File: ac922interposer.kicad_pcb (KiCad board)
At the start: 2 copper layers, 15 parts, among them J1 2336568-1, U1 molex_impact_85ohm_left_and_r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

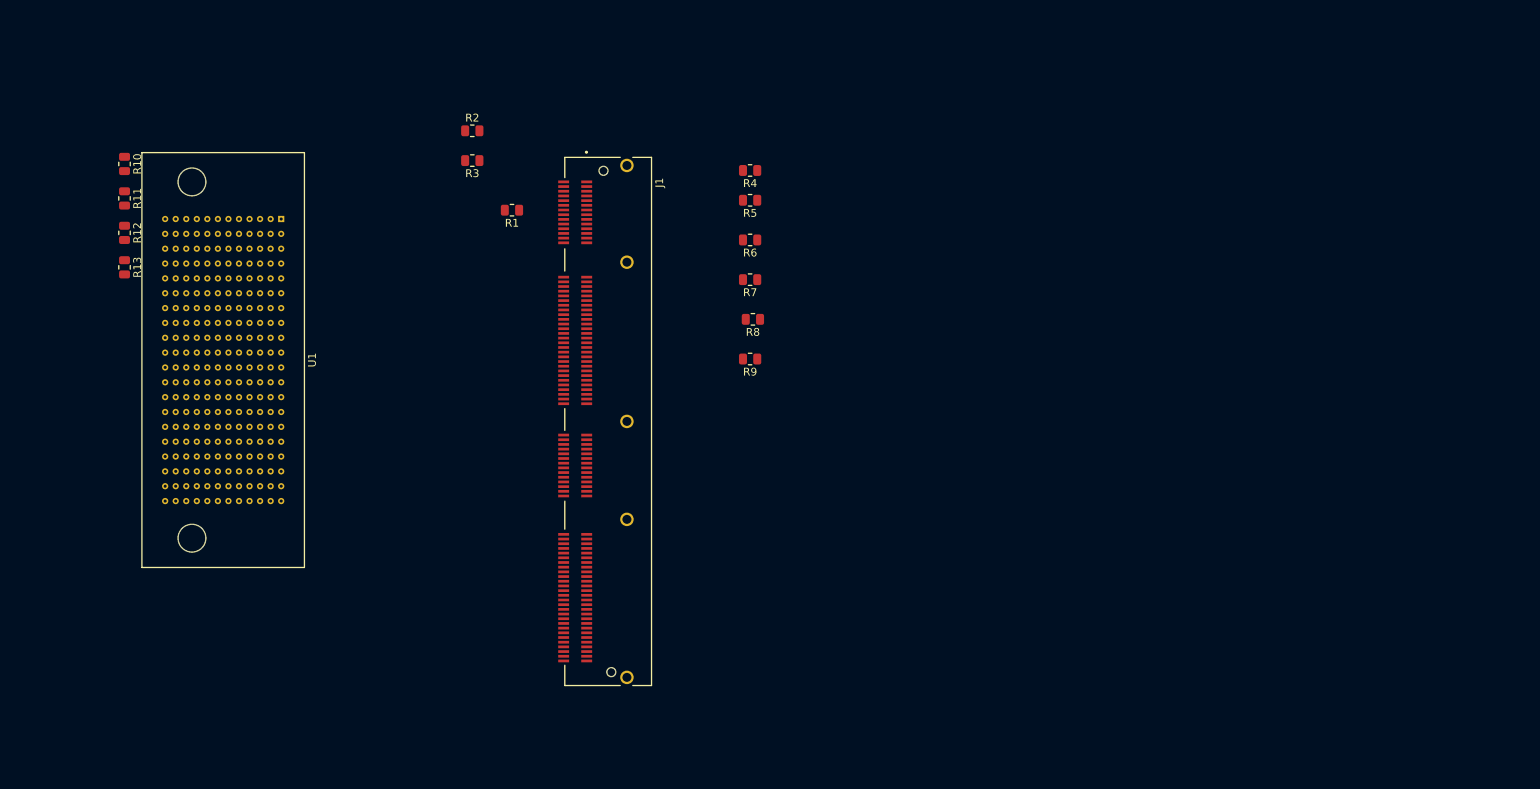
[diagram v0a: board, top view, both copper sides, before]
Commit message: Placement, initial holes, and some traces.
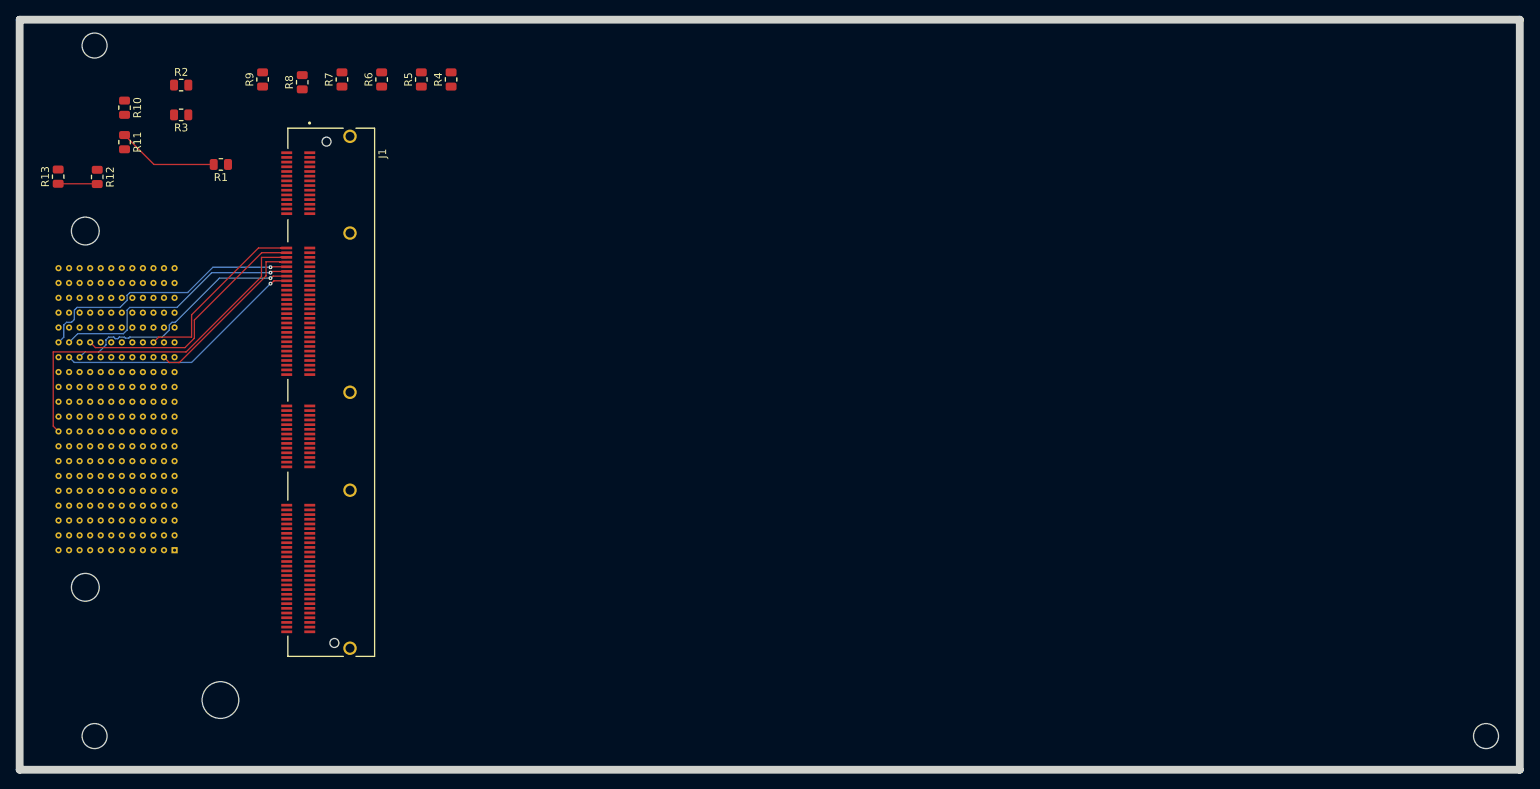
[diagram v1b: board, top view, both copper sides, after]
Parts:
- U1: moved to B.Cu
- moved R9 71.9 mm to (80.8, 67.1), turned to 90 degrees
- moved R8 65.2 mm to (85.8, 67.4), turned to 90 degrees
- moved U1 60.9 mm to (51.7, 135.8), turned to 90 degrees
- moved R7 58.2 mm to (90.9, 67.1), turned to 90 degrees
- moved R6 51.4 mm to (96.0, 67.1), turned to 90 degrees
- moved R5 44.8 mm to (101.1, 67.1), turned to 90 degrees
- moved R4 40.0 mm to (104.9, 67.1), turned to 90 degrees
- moved R1 37.7 mm to (75.4, 78.0)
- moved R2 37.7 mm to (70.3, 67.8)
- moved R3 37.7 mm to (70.3, 71.6)
- moved J1 35.6 mm to (88.9, 107.1)
- moved R13 14.4 mm to (54.6, 79.5), turned to 90 degrees
- moved R12 7.97 mm to (59.6, 79.6)
- moved R10 7.20 mm to (63.1, 70.7)
- moved R11 7.20 mm to (63.1, 75.1)
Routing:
- net ESPI_ALERT_N: track 0.00 -> 48.4 mm
- net ESPI_IO0: track 0.00 -> 35.2 mm, vias 0 -> 1
- net ESPI_IO1: track 0.00 -> 33.1 mm, vias 0 -> 1
- net ESPI_CS0_N: track 0.00 -> 32.6 mm
- net ESPI_IO3: track 0.00 -> 32.5 mm, vias 0 -> 1
- net ESPI_IO2: track 0.00 -> 31.8 mm, vias 0 -> 1
- net ESPI_CLK: track 0.00 -> 24.5 mm
- net ESPI_RESET_N: track 0.00 -> 22.6 mm
- net +3.3VCS: track 0.00 -> 13.0 mm
- net /Sequoia Connections/12VCS_RESET_N: track 0.00 -> 5.02 mm
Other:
- board outline added: 192 x 96 mm
- copper layers 2 -> 4
- net class Default: trace_width 0.25 -> 0.15; via_dia 0.8 -> 0.5; via_drill 0.4 -> 0.2
- rule trace_min: 0.2 -> 0.1
- rule via_min_drill: 0.3 -> 0.2
- board text added: "U"
- board text added: "W"

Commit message: Update some routes.  Perhaps some schematic.
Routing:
- net GND: track 0.00 -> 246.8 mm
- net I2C3_SDA: track 0.00 -> 50.3 mm, vias 0 -> 2
- net I2C3_SCL: track 0.00 -> 50.1 mm, vias 0 -> 2
- net I3C3_SDA: track 0.00 -> 48.4 mm, vias 0 -> 2
- net I2C2_SDA: track 0.00 -> 46.1 mm, vias 0 -> 1
- net I3C3_SCL: track 0.00 -> 45.9 mm, vias 0 -> 2
- net I2C4_SCL: track 0.00 -> 45.8 mm, vias 0 -> 2
- net I2C4_SDA: track 0.00 -> 44.7 mm, vias 0 -> 2
- net I2C2_SCL: track 0.00 -> 43.9 mm, vias 0 -> 1
- net I2C1_SDA: track 0.00 -> 39.3 mm, vias 0 -> 1
- net I2C6_SCL: track 0.00 -> 38.2 mm, vias 0 -> 2
- net I2C6_SDA: track 0.00 -> 37.9 mm, vias 0 -> 2
- net I2C5_SDA: track 0.00 -> 37.5 mm, vias 0 -> 1
- net I2C12_SDA: track 0.00 -> 37.4 mm
- net I2C1_SCL: track 0.00 -> 36.8 mm, vias 0 -> 1
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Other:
- board size 192 x 96 mm -> 192.1 x 96 mm
- copper layers 4 -> 6
- board text added: "S"
- board text added: "V"
